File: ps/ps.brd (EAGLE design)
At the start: 99.1 x 54.6 mm, 66 parts, among them IC1 LM675, Q1 NPN-D, Q2 NPN-D, U1 LM3480IM4, U2 LM317, U3 TLC555CD, U4 LM317, U5 LM317

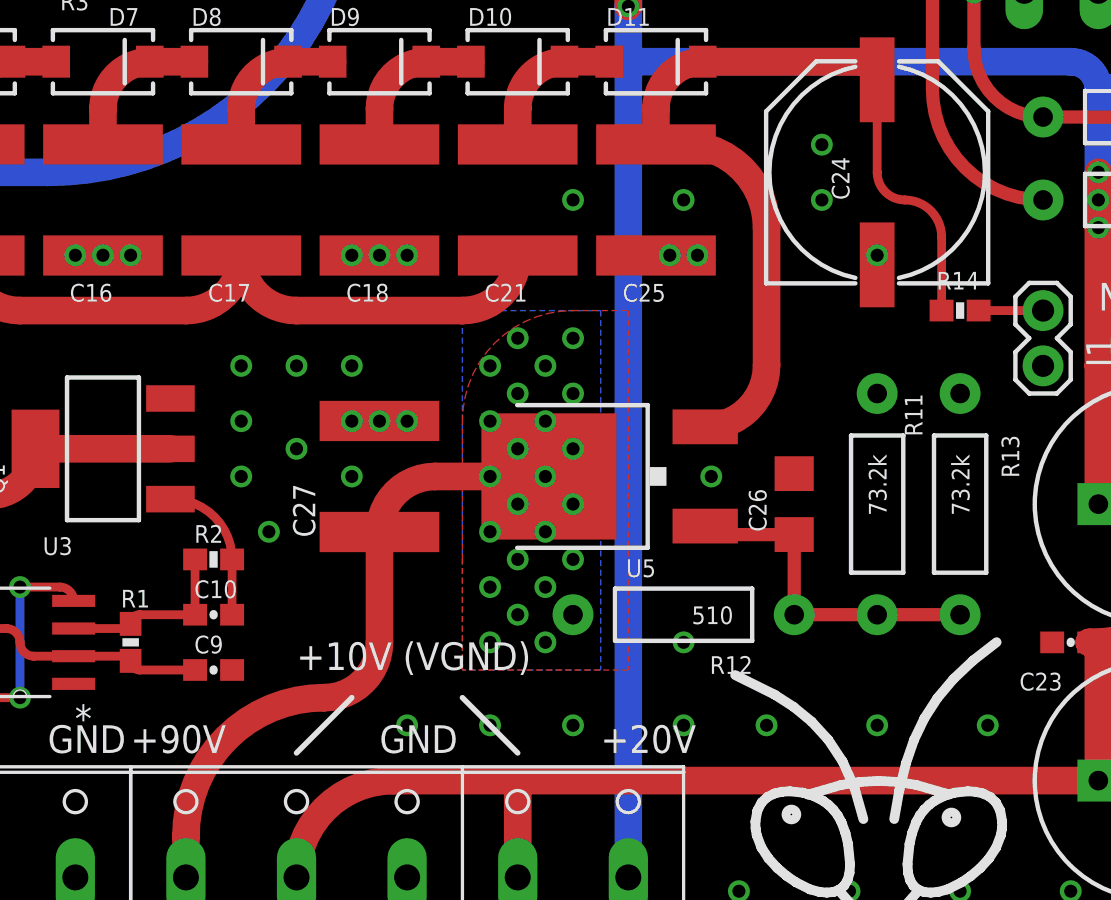
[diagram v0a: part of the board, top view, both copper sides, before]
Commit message: Back to 60V supply
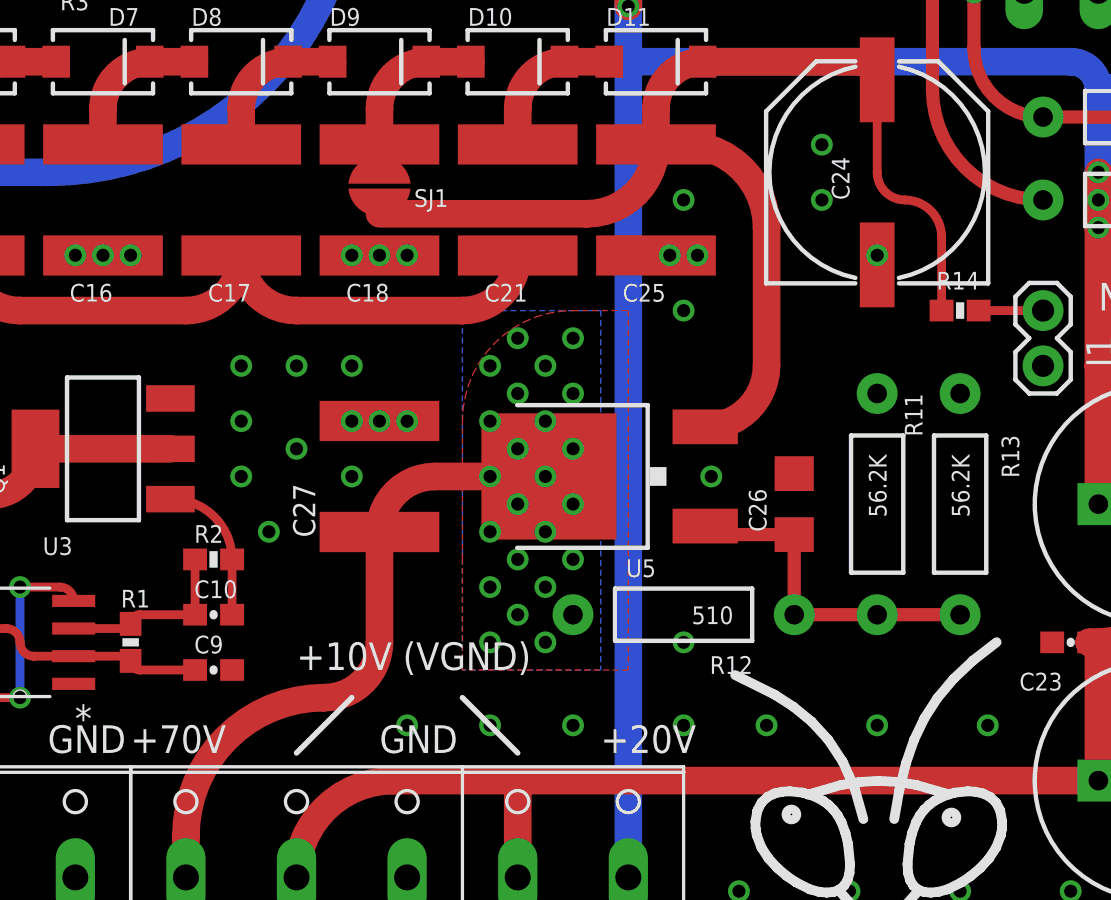
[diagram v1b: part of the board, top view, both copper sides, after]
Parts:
- added SJ1: (no value), my:SJ_ROUND_NOPLACE
- R11, R13: value 73.2k -> 56.2K
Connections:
- net HV: now also SJ1.2
- net N$15: now also SJ1.1
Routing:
- net HV: track 41.9 -> 55.9 mm
- net N$15: track 6.74 -> 7.39 mm
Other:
- board text added: "+70V"
- board text removed: "+90V"
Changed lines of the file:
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@@
 <text x="38.1" y="10.16" size="1.27" layer="21" font="vector" ratio="15">GND</text>
 <text x="29.21" y="10.16" size="1.27" layer="21" font="vector" ratio="15">HEATER</text>
-<text x="41.91" y="10.16" size="1.27" layer="21" font="vector" ratio="15">+90V</text>
+<text x="41.91" y="10.16" size="1.27" layer="21" font="vector" ratio="15">+70V</text>
 <text x="53.34" y="10.16" size="1.27" layer="21" font="vector" ratio="15">GND</text>
 <text x="49.53" y="13.97" size="1.27" layer="21" font="vector" ratio="15">+10V (VGND)</text>
@@
 <attribute name="VALUE" x="30.861" y="20.828" size="0.8128" layer="27" font="vector" ratio="15" rot="R180"/>
 </element>
-<element name="R11" library="SparkFun-Resistors" package="AXIAL-0.4" value="73.2k" x="76.2" y="21.59" smashed="yes" rot="R270">
+<element name="R11" library="SparkFun-Resistors" package="AXIAL-0.4" value="56.2K" x="76.2" y="21.59" smashed="yes" rot="R270">
 <attribute name="NAME" x="77.47" y="26.67" size="0.8128" layer="25" font="vector" ratio="15" rot="R270"/>
 <attribute name="VALUE" x="75.819" y="23.876" size="0.8128" layer="21" font="vector" ratio="15" rot="R270"/>
 </element>
-<element name="R13" library="SparkFun-Resistors" package="AXIAL-0.4" value="73.2k" x="80.01" y="21.59" rot="R270"/>
+<element name="R13" library="SparkFun-Resistors" package="AXIAL-0.4" value="56.2K" x="80.01" y="21.59" rot="R270"/>
 <element name="R12" library="SparkFun-Resistors" package="AXIAL-0.4" value="510" x="67.31" y="16.51" rot="R180"/>
 <element name="U3" library="Texas Instruments_By_element14_Batch_1" package="SOIC127P600X175-8N" value="TLC555CD" x="36.83" y="15.24" smashed="yes" rot="R180">
@@
 <attribute name="NAME" x="80.899" y="32.258" size="0.8128" layer="25" font="vector" ratio="15" rot="R180"/>
 <attribute name="VALUE" x="79.121" y="29.718" size="0.8128" layer="27" font="vector" ratio="15" rot="R180"/>
+</element>
+<element name="SJ1" library="my" package="SJ_ROUND_NOPLACE" value="" x="53.34" y="36.195" smashed="yes" rot="R270">
+<attribute name="NAME" x="54.9275" y="35.2425" size="0.8128" layer="25" ratio="15"/>
+<attribute name="VALUE" x="49.8475" y="39.37" size="1.27" layer="27" rot="R270"/>
 </element>
 </elements>
@@
 <via x="67.31" y="15.24" extent="1-16" drill="0.6"/>
 <via x="67.31" y="11.43" extent="1-16" drill="0.6"/>
-<via x="67.31" y="35.56" extent="1-16" drill="0.6"/>
-<via x="62.23" y="35.56" extent="1-16" drill="0.6"/>
 <via x="68.58" y="22.86" extent="1-16" drill="0.6"/>
 <via x="58.42" y="11.43" extent="1-16" drill="0.6"/>
@@
 <via x="73.66" y="38.1" extent="1-16" drill="0.6"/>
 <via x="76.2" y="33.02" extent="1-16" drill="0.6"/>
+<via x="67.31" y="35.56" extent="1-16" drill="0.6"/>
+<via x="67.31" y="30.48" extent="1-16" drill="0.6"/>
 </signal>
 <signal name="555CONT">
@@
 <wire x1="53.34" y1="39.76" x2="55.49" y2="41.91" width="1.27" layer="1" curve="-90"/>
 <wire x1="55.49" y1="41.91" x2="57.54" y2="41.91" width="1.27" layer="1"/>
+<contactref element="SJ1" pad="1"/>
+<wire x1="53.34" y1="37.465" x2="53.34" y2="38.11" width="1.27" layer="1"/>
 </signal>
 <signal name="PUMPIN" class="1">
@@
 <wire x1="71.12" y1="27.96" x2="71.12" y2="34.29" width="1.27" layer="1"/>
 <wire x1="71.12" y1="34.29" x2="67.3" y2="38.11" width="1.27" layer="1" curve="90"/>
+<contactref element="SJ1" pad="2"/>
+<wire x1="53.34" y1="34.925" x2="62.855" y2="34.925" width="1.27" layer="1"/>
+<wire x1="62.855" y1="34.925" x2="66.04" y2="38.11" width="1.27" layer="1" curve="90"/>
 </signal>
 <signal name="N$18">

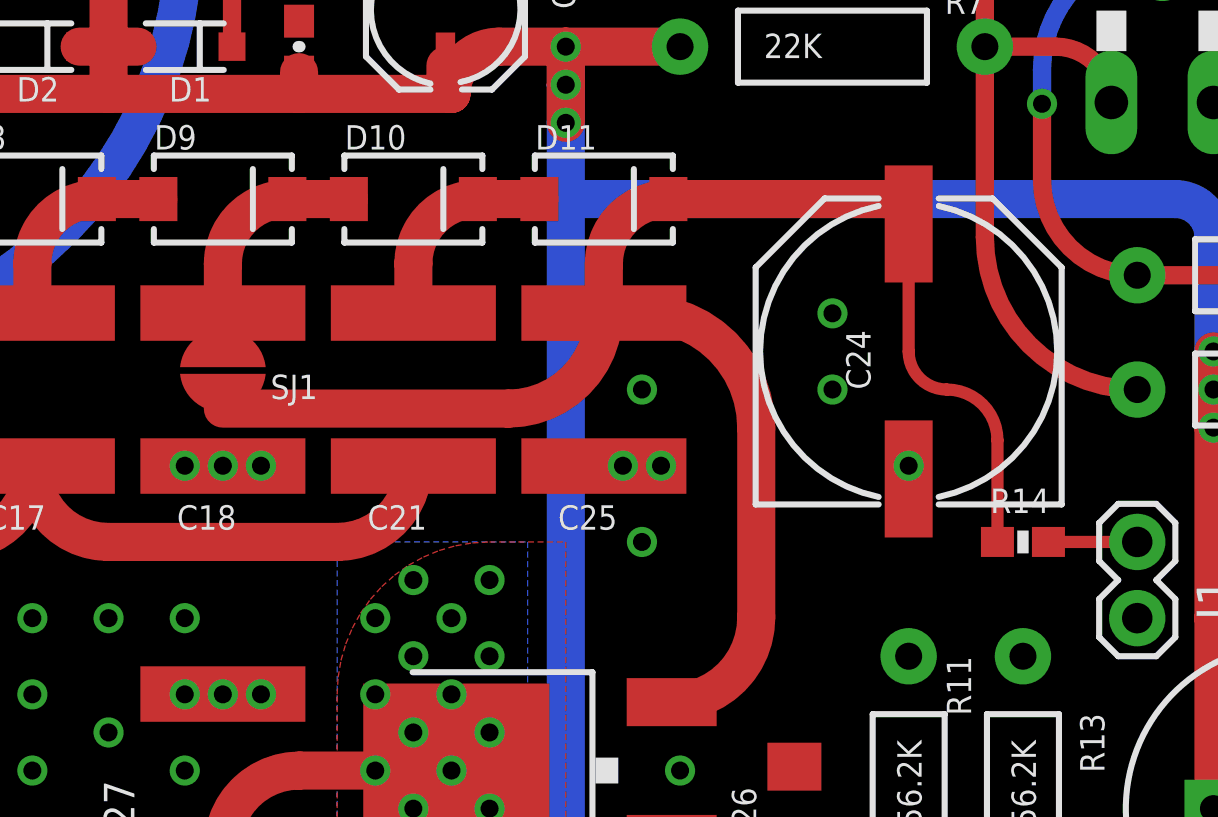
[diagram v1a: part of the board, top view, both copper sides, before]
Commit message: HV for neon bulb
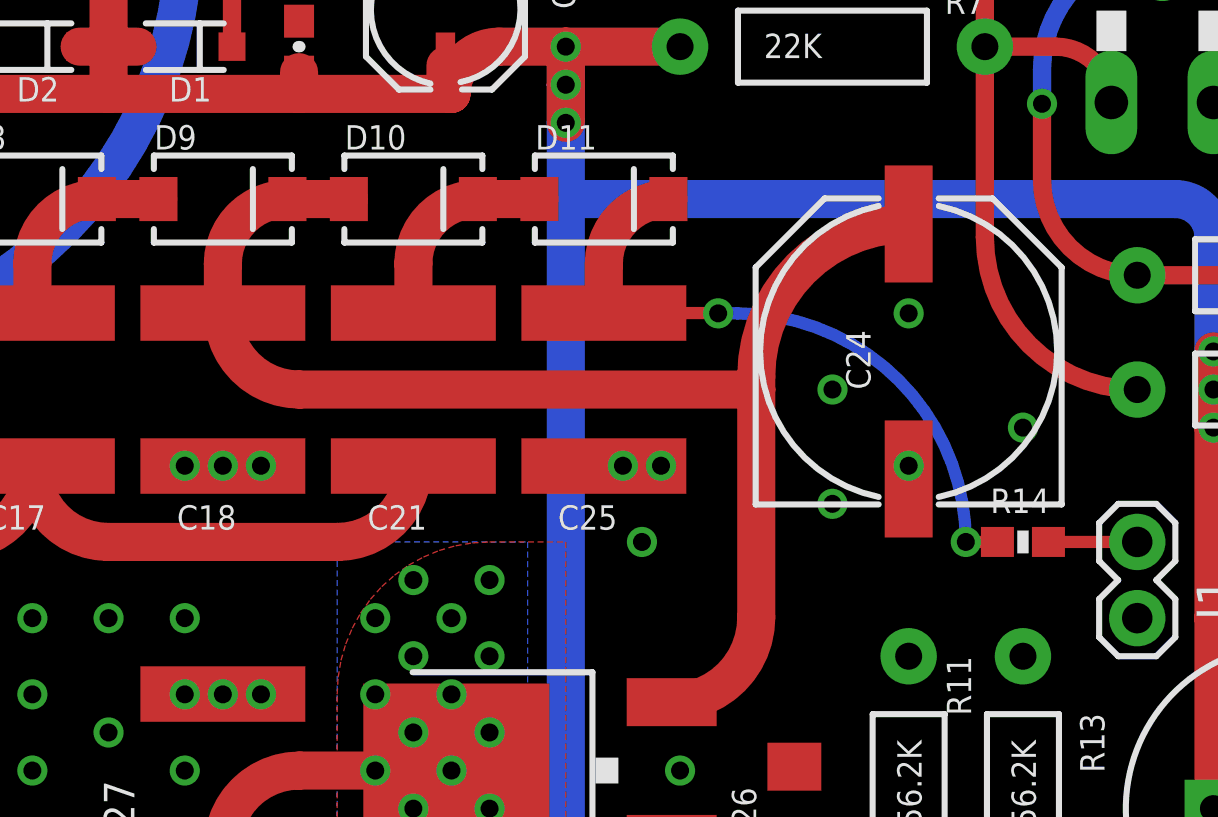
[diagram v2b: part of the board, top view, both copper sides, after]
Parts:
- removed SJ1: (no value), my:SJ_ROUND_NOPLACE
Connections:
- net HV: no longer C24.+, SJ1.2, U5.3
- net N$15: now also C24.+, U5.3; no longer SJ1.1
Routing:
- net N$15: track 7.39 -> 44.8 mm
- net HV: track 55.9 -> 21.0 mm, vias 0 -> 2
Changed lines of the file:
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@@
 <hole x="95.25" y="50.8" drill="3.2"/>
 <hole x="95.25" y="3.81" drill="3.2"/>
-<dimension x1="0" y1="54.61" x2="99.06" y2="54.61" x3="49.53" y3="59.69" textsize="1.778" layer="47"/>
-<dimension x1="0" y1="0" x2="0" y2="54.61" x3="-5.08" y3="27.305" textsize="1.778" layer="47"/>
+<dimension x1="0" y1="54.61" x2="99.06" y2="54.61" x3="49.53" y3="59.69" textsize="1.27" layer="47"/>
+<dimension x1="0" y1="0" x2="0" y2="54.61" x3="-5.08" y3="27.305" textsize="1.27" layer="47"/>
 <text x="5.08" y="10.16" size="1.27" layer="21" font="vector" ratio="15">+24V VCC</text>
 <text x="17.78" y="10.16" size="1.27" layer="21" font="vector" ratio="15">GND</text>
@@
 <wire x1="59.69" y1="10.16" x2="57.15" y2="12.7" width="0.254" layer="21"/>
 <text x="86.36" y="30.48" size="1.27" layer="21" font="vector" ratio="15">NE-2 lamp</text>
+<dimension x1="0" y1="0" x2="49.53" y2="0" x3="24.765" y3="-6.35" textsize="1.27" layer="47"/>
 </plain>
 <attributes>
@@
 <attribute name="VALUE" x="79.121" y="29.718" size="0.8128" layer="27" font="vector" ratio="15" rot="R180"/>
 </element>
-<element name="SJ1" library="my" package="SJ_ROUND_NOPLACE" value="" x="53.34" y="36.195" smashed="yes" rot="R270">
-<attribute name="NAME" x="54.9275" y="35.2425" size="0.8128" layer="25" ratio="15"/>
-<attribute name="VALUE" x="49.8475" y="39.37" size="1.27" layer="27" rot="R270"/>
-</element>
 </elements>
 <signals>
@@
 <contactref element="J1" pad="1"/>
 <via x="73.66" y="35.56" extent="1-16" drill="0.6"/>
-<via x="73.66" y="38.1" extent="1-16" drill="0.6"/>
+<via x="76.2" y="38.1" extent="1-16" drill="0.6"/>
 <via x="76.2" y="33.02" extent="1-16" drill="0.6"/>
-<via x="67.31" y="35.56" extent="1-16" drill="0.6"/>
 <via x="67.31" y="30.48" extent="1-16" drill="0.6"/>
+<via x="73.66" y="31.75" extent="1-16" drill="0.6"/>
+<via x="80.01" y="34.29" extent="1-16" drill="0.6"/>
 </signal>
 <signal name="555CONT">
@@
 <wire x1="53.34" y1="39.76" x2="55.49" y2="41.91" width="1.27" layer="1" curve="-90"/>
 <wire x1="55.49" y1="41.91" x2="57.54" y2="41.91" width="1.27" layer="1"/>
-<contactref element="SJ1" pad="1"/>
-<wire x1="53.34" y1="37.465" x2="53.34" y2="38.11" width="1.27" layer="1"/>
+<contactref element="U5" pad="3"/>
+<contactref element="C24" pad="+"/>
+<wire x1="68.3" y1="25.14" x2="71.12" y2="27.96" width="1.27" layer="1" curve="90"/>
+<wire x1="71.12" y1="27.96" x2="71.12" y2="35.56" width="1.27" layer="1"/>
+<wire x1="71.12" y1="35.56" x2="71.12" y2="36" width="1.27" layer="1"/>
+<wire x1="71.12" y1="36" x2="76.2" y2="41.08" width="1.27" layer="1" curve="-90"/>
+<wire x1="53.34" y1="38.11" x2="55.89" y2="35.56" width="1.27" layer="1" curve="90"/>
+<wire x1="55.89" y1="35.56" x2="71.12" y2="35.56" width="1.27" layer="1"/>
 </signal>
 <signal name="PUMPIN" class="1">
@@
 <signal name="HV" class="1">
 <contactref element="D11" pad="C"/>
-<contactref element="C24" pad="+"/>
-<contactref element="U5" pad="3"/>
 <contactref element="C25" pad="1"/>
 <wire x1="66.04" y1="38.11" x2="66.04" y2="39.76" width="1.27" layer="1"/>
 <wire x1="66.04" y1="39.76" x2="68.19" y2="41.91" width="1.27" layer="1" curve="-90"/>
-<wire x1="68.19" y1="41.91" x2="75.37" y2="41.91" width="1.27" layer="1"/>
-<wire x1="75.37" y1="41.91" x2="76.2" y2="41.08" width="1.27" layer="1" curve="-90"/>
 <wire x1="66.04" y1="38.11" x2="67.3" y2="38.11" width="1.27" layer="1"/>
 <contactref element="R14" pad="2"/>
-<wire x1="79.16" y1="30.48" x2="79.16" y2="33.87" width="0.4064" layer="1"/>
-<wire x1="79.16" y1="33.87" x2="77.47" y2="35.56" width="0.4064" layer="1" curve="90"/>
-<wire x1="77.47" y1="35.56" x2="76.2" y2="36.83" width="0.4064" layer="1" curve="-90"/>
-<wire x1="76.2" y1="36.83" x2="76.2" y2="41.08" width="0.4064" layer="1"/>
-<wire x1="68.3" y1="25.14" x2="71.12" y2="27.96" width="1.27" layer="1" curve="90"/>
-<wire x1="71.12" y1="27.96" x2="71.12" y2="34.29" width="1.27" layer="1"/>
-<wire x1="71.12" y1="34.29" x2="67.3" y2="38.11" width="1.27" layer="1" curve="90"/>
-<contactref element="SJ1" pad="2"/>
-<wire x1="53.34" y1="34.925" x2="62.855" y2="34.925" width="1.27" layer="1"/>
-<wire x1="62.855" y1="34.925" x2="66.04" y2="38.11" width="1.27" layer="1" curve="90"/>
+<wire x1="79.16" y1="30.48" x2="78.105" y2="30.48" width="0.4064" layer="1"/>
+<via x="78.105" y="30.48" extent="1-16" drill="0.6"/>
+<wire x1="78.105" y1="30.48" x2="70.485" y2="38.1" width="0.4064" layer="16" curve="90"/>
+<wire x1="70.485" y1="38.1" x2="69.85" y2="38.1" width="0.4064" layer="16"/>
+<via x="69.85" y="38.1" extent="1-16" drill="0.6"/>
+<wire x1="69.85" y1="38.1" x2="69.84" y2="38.11" width="0.4064" layer="1" curve="90"/>
+<wire x1="69.84" y1="38.11" x2="67.3" y2="38.11" width="0.4064" layer="1"/>
 </signal>
 <signal name="N$18">
